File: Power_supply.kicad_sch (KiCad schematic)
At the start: 16 parts, among them J2 DC_DC_Buck_converter_module, U1 TPS562201DDCR

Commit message: wip
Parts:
- renumbered C74 to C14, C75 to C15, C76 to C16, C77 to C17, C78 to C18, C79 to C19, C80 to C20, L13 to L1, R41 to R5, R42 to R6, R43 to R7, R44 to R8
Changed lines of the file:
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@@
 		(on_board yes)
 		(dnp no)
-		(property "Reference" "#PWR0172"
+		(property "Reference" "#PWR064"
 			(at 55.88 88.9 0)
 			(effects
@@
 			(project "mgr_board"
 				(path "/14d3b6cb-e4ae-41db-89eb-e86b07bc47b0/1fa8a5b5-8827-4ec4-a071-93d7f03057ab"
-					(reference "#PWR0172")
+					(reference "#PWR064")
 					(unit 1)
 				)
@@
 		(dnp no)
 		(fields_autoplaced yes)
-		(property "Reference" "R43"
+		(property "Reference" "R7"
 			(at 151.13 87.6299 90)
 			(effects
@@
 			(project "mgr_board"
 				(path "/14d3b6cb-e4ae-41db-89eb-e86b07bc47b0/1fa8a5b5-8827-4ec4-a071-93d7f03057ab"
-					(reference "R43")
+					(reference "R7")
 					(unit 1)
 				)
@@
 		(dnp no)
 		(fields_autoplaced yes)
-		(property "Reference" "R42"
+		(property "Reference" "R6"
 			(at 96.52 97.7899 90)
 			(effects
@@
 			(project "mgr_board"
 				(path "/14d3b6cb-e4ae-41db-89eb-e86b07bc47b0/1fa8a5b5-8827-4ec4-a071-93d7f03057ab"
-					(reference "R42")
+					(reference "R6")
 					(unit 1)
 				)
@@
 		(on_board yes)
 		(dnp no)
-		(property "Reference" "C76"
+		(property "Reference" "C16"
 			(at 78.994 89.662 0)
 			(effects
@@
 			(project "mgr_board"
 				(path "/14d3b6cb-e4ae-41db-89eb-e86b07bc47b0/1fa8a5b5-8827-4ec4-a071-93d7f03057ab"
-					(reference "C76")
+					(reference "C16")
 					(unit 1)
 				)
@@
 		(dnp no)
 		(fields_autoplaced yes)
-		(property "Reference" "#PWR0173"
+		(property "Reference" "#PWR065"
 			(at 60.96 96.52 0)
 			(effects
@@
 			(project "mgr_board"
 				(path "/14d3b6cb-e4ae-41db-89eb-e86b07bc47b0/1fa8a5b5-8827-4ec4-a071-93d7f03057ab"
-					(reference "#PWR0173")
+					(reference "#PWR065")
 					(unit 1)
 				)
@@
 		(dnp no)
 		(fields_autoplaced yes)
-		(property "Reference" "#PWR0179"
+		(property "Reference" "#PWR071"
 			(at 114.3 101.6 0)
 			(effects
@@
 			(project "mgr_board"
 				(path "/14d3b6cb-e4ae-41db-89eb-e86b07bc47b0/1fa8a5b5-8827-4ec4-a071-93d7f03057ab"
-					(reference "#PWR0179")
+					(reference "#PWR071")
 					(unit 1)
 				)
@@
 		(on_board yes)
 		(dnp no)
-		(property "Reference" "#PWR0185"
+		(property "Reference" "#PWR077"
 			(at 190.5 88.9 0)
 			(effects
@@
 			(project "mgr_board"
 				(path "/14d3b6cb-e4ae-41db-89eb-e86b07bc47b0/1fa8a5b5-8827-4ec4-a071-93d7f03057ab"
-					(reference "#PWR0185")
+					(reference "#PWR077")
 					(unit 1)
 				)
@@
 		(dnp no)
 		(fields_autoplaced yes)
-		(property "Reference" "#PWR0183"
+		(property "Reference" "#PWR075"
 			(at 176.53 96.52 0)
 			(effects
@@
 			(project "mgr_board"
 				(path "/14d3b6cb-e4ae-41db-89eb-e86b07bc47b0/1fa8a5b5-8827-4ec4-a071-93d7f03057ab"
-					(reference "#PWR0183")
+					(reference "#PWR075")
 					(unit 1)
 				)
@@
 		(dnp no)
 		(fields_autoplaced yes)
-		(property "Reference" "R44"
+		(property "Reference" "R8"
 			(at 151.13 97.7899 90)
 			(effects
@@
 			(project "mgr_board"
 				(path "/14d3b6cb-e4ae-41db-89eb-e86b07bc47b0/1fa8a5b5-8827-4ec4-a071-93d7f03057ab"
-					(reference "R44")
+					(reference "R8")
 					(unit 1)
 				)
@@
 		(dnp no)
 		(fields_autoplaced yes)
-		(property "Reference" "#PWR0182"
+		(property "Reference" "#PWR074"
 			(at 166.37 96.52 0)
 			(effects
@@
 			(project "mgr_board"
 				(path "/14d3b6cb-e4ae-41db-89eb-e86b07bc47b0/1fa8a5b5-8827-4ec4-a071-93d7f03057ab"
-					(reference "#PWR0182")
+					(reference "#PWR074")
 					(unit 1)
 				)
@@
 		(on_board yes)
 		(dnp no)
-		(property "Reference" "C74"
+		(property "Reference" "C14"
 			(at 56.388 89.662 0)
 			(effects
@@
 			(project "mgr_board"
 				(path "/14d3b6cb-e4ae-41db-89eb-e86b07bc47b0/1fa8a5b5-8827-4ec4-a071-93d7f03057ab"
-					(reference "C74")
+					(reference "C14")
 					(unit 1)
 				)
@@
 		(on_board yes)
 		(dnp no)
-		(property "Reference" "C80"
+		(property "Reference" "C20"
 			(at 194.056 88.646 0)
 			(effects
@@
 			(project "mgr_board"
 				(path "/14d3b6cb-e4ae-41db-89eb-e86b07bc47b0/1fa8a5b5-8827-4ec4-a071-93d7f03057ab"
-					(reference "C80")
+					(reference "C20")
 					(unit 1)
 				)
@@
 		(on_board yes)
 		(dnp no)
-		(property "Reference" "#PWR0180"
+		(property "Reference" "#PWR072"
 			(at 121.92 67.31 0)
 			(effects
@@
 			(project "mgr_board"
 				(path "/14d3b6cb-e4ae-41db-89eb-e86b07bc47b0/1fa8a5b5-8827-4ec4-a071-93d7f03057ab"
-					(reference "#PWR0180")
+					(reference "#PWR072")
 					(unit 1)
 				)
@@
 		(dnp no)
 		(fields_autoplaced yes)
-		(property "Reference" "#PWR0175"
+		(property "Reference" "#PWR067"
 			(at 83.82 96.52 0)
 			(effects
@@
 			(project "mgr_board"
 				(path "/14d3b6cb-e4ae-41db-89eb-e86b07bc47b0/1fa8a5b5-8827-4ec4-a071-93d7f03057ab"
-					(reference "#PWR0175")
+					(reference "#PWR067")
 					(unit 1)
 				)
@@
 		(dnp no)
 		(fields_autoplaced yes)
-		(property "Reference" "#PWR0184"
+		(property "Reference" "#PWR076"
 			(at 186.69 96.52 0)
 			(effects
@@
 			(project "mgr_board"
 				(path "/14d3b6cb-e4ae-41db-89eb-e86b07bc47b0/1fa8a5b5-8827-4ec4-a071-93d7f03057ab"
-					(reference "#PWR0184")
+					(reference "#PWR076")
 					(unit 1)
 				)
@@
 		(on_board yes)
 		(dnp no)
-		(property "Reference" "C77"
+		(property "Reference" "C17"
 			(at 138.684 91.186 0)
 			(effects
@@
 			(project "mgr_board"
 				(path "/14d3b6cb-e4ae-41db-89eb-e86b07bc47b0/1fa8a5b5-8827-4ec4-a071-93d7f03057ab"
-					(reference "C77")
+					(reference "C17")
 					(unit 1)
 				)
@@
 		(on_board yes)
 		(dnp no)
-		(property "Reference" "C78"
+		(property "Reference" "C18"
 			(at 172.974 88.9 0)
 			(effects
@@
 			(project "mgr_board"
 				(path "/14d3b6cb-e4ae-41db-89eb-e86b07bc47b0/1fa8a5b5-8827-4ec4-a071-93d7f03057ab"
-					(reference "C78")
+					(reference "C18")
 					(unit 1)
 				)
@@
 		(dnp no)
 		(fields_autoplaced yes)
-		(property "Reference" "#PWR0174"
+		(property "Reference" "#PWR066"
 			(at 71.12 96.52 0)
 			(effects
@@
 			(project "mgr_board"
 				(path "/14d3b6cb-e4ae-41db-89eb-e86b07bc47b0/1fa8a5b5-8827-4ec4-a071-93d7f03057ab"
-					(reference "#PWR0174")
+					(reference "#PWR066")
 					(unit 1)
 				)
@@
 		(dnp no)
 		(fields_autoplaced yes)
-		(property "Reference" "#PWR0178"
+		(property "Reference" "#PWR070"
 			(at 114.3 72.39 0)
 			(effects
@@
 			(project "mgr_board"
 				(path "/14d3b6cb-e4ae-41db-89eb-e86b07bc47b0/1fa8a5b5-8827-4ec4-a071-93d7f03057ab"
-					(reference "#PWR0178")
+					(reference "#PWR070")
 					(unit 1)
 				)
@@
 		(on_board yes)
 		(dnp no)
-		(property "Reference" "#PWR0177"
+		(property "Reference" "#PWR069"
 			(at 106.68 67.31 0)
 			(effects
@@
 			(project "mgr_board"
 				(path "/14d3b6cb-e4ae-41db-89eb-e86b07bc47b0/1fa8a5b5-8827-4ec4-a071-93d7f03057ab"
-					(reference "#PWR0177")
+					(reference "#PWR069")
 					(unit 1)
 				)
@@
 		(dnp no)
 		(fields_autoplaced yes)
-		(property "Reference" "L13"
+		(property "Reference" "L1"
 			(at 139.7 80.01 90)
 			(effects
@@
 			(project ""
 				(path "/14d3b6cb-e4ae-41db-89eb-e86b07bc47b0/1fa8a5b5-8827-4ec4-a071-93d7f03057ab"
-					(reference "L13")
+					(reference "L1")
 					(unit 1)
 				)
@@
 		(on_board yes)
 		(dnp no)
-		(property "Reference" "C79"
+		(property "Reference" "C19"
 			(at 182.88 89.408 0)
 			(effects
@@
 			(project "mgr_board"
 				(path "/14d3b6cb-e4ae-41db-89eb-e86b07bc47b0/1fa8a5b5-8827-4ec4-a071-93d7f03057ab"
-					(reference "C79")
+					(reference "C19")
 					(unit 1)
 				)
@@
 		(dnp no)
 		(fields_autoplaced yes)
-		(property "Reference" "#PWR0176"
+		(property "Reference" "#PWR068"
 			(at 93.98 109.22 0)
 			(effects
@@
 			(project "mgr_board"
 				(path "/14d3b6cb-e4ae-41db-89eb-e86b07bc47b0/1fa8a5b5-8827-4ec4-a071-93d7f03057ab"
-					(reference "#PWR0176")
+					(reference "#PWR068")
 					(unit 1)
 				)
@@
 		(on_board yes)
 		(dnp no)
-		(property "Reference" "C75"
+		(property "Reference" "C15"
 			(at 67.056 89.662 0)
 			(effects
@@
 			(project "mgr_board"
 				(path "/14d3b6cb-e4ae-41db-89eb-e86b07bc47b0/1fa8a5b5-8827-4ec4-a071-93d7f03057ab"
-					(reference "C75")
+					(reference "C15")
 					(unit 1)
 				)
@@
 		(dnp no)
 		(fields_autoplaced yes)
-		(property "Reference" "#PWR0181"
+		(property "Reference" "#PWR073"
 			(at 148.59 109.22 0)
 			(effects
@@
 			(project "mgr_board"
 				(path "/14d3b6cb-e4ae-41db-89eb-e86b07bc47b0/1fa8a5b5-8827-4ec4-a071-93d7f03057ab"
-					(reference "#PWR0181")
+					(reference "#PWR073")
 					(unit 1)
 				)
@@
 		(dnp no)
 		(fields_autoplaced yes)
-		(property "Reference" "R41"
+		(property "Reference" "R5"
 			(at 96.52 87.6299 90)
 			(effects
@@
 			(project "mgr_board"
 				(path "/14d3b6cb-e4ae-41db-89eb-e86b07bc47b0/1fa8a5b5-8827-4ec4-a071-93d7f03057ab"
-					(reference "R41")
-					(unit 1)
-				)
+					(reference "R5")
+					(unit 1)
+				)

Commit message: wip
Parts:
- removed J2: DC_DC_Buck_converter_module, Connector_PinHeader_2.54mm:PinHeader_1x03_P2.54mm_Vertical, symbol PCM_SL_Pin_Headers:PINHD_1x3_Male
- added U2: LM2596 BUCK MODULE, footprint_lib:LM2596 DC-DC module, symbol sym_lib:DC-DC_Step_down_module
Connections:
- net +12V: now also U2.1 (IN+)
- net +5V: now also U2.3 (OUT+)
- net GND: now also U2.2 (IN-), U2.4 (OUT-)
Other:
- note added: "OPTIONAL"

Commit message: finished boarD
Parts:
- removed TP21: TestPoint, TestPoint:TestPoint_Pad_D2.0mm, symbol Connector:TestPoint
- added C83, C84: 100uF, Capacitor_SMD:CP_Elec_6.3x7.7, symbol Device:C_Polarized_Small
- C14, C18: LCSC (none) -> C96446
- C15, C19: LCSC (none) -> C45783
- C16, C17, C20: LCSC (none) -> C14663
- L1: LCSC (none) -> C408410
- R5, R6, R8: LCSC (none) -> C25804
- R7: value 54,9k -> 56k; LCSC (none) -> C23206
- U1: LCSC (none) -> C90061
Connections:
- net +12V: now also C83.1, C84.1
- net GND: now also C83.2, C84.2

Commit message: Fixed bugs after reviews
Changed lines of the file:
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@@
 					(size 1.27 1.27)
 				)
+				(hide yes)
 			)
 		)
@@
 					(size 1.27 1.27)
 				)
+				(hide yes)
 			)
 		)
@@
 					(size 1.27 1.27)
 				)
+				(hide yes)
 			)
 		)
@@
 					(size 1.27 1.27)
 				)
+				(hide yes)
 			)
 		)
@@
 					(size 1.27 1.27)
 				)
+				(hide yes)
 			)
 		)
@@
 					(size 1.27 1.27)
 				)
+				(hide yes)
 			)
 		)
@@
 					(size 1.27 1.27)
 				)
+				(hide yes)
 			)
 		)
@@
 					(size 1.27 1.27)
 				)
+				(hide yes)
 			)
 		)
@@
 					(size 1.27 1.27)
 				)
+				(hide yes)
 			)
 		)
@@
 					(size 1.27 1.27)
 				)
+				(hide yes)
 			)
 		)
@@
 					(size 1.27 1.27)
 				)
+				(hide yes)
 			)
 		)
@@
 					(size 1.27 1.27)
 				)
-			)
-		)
+				(hide yes)
+			)
+		)

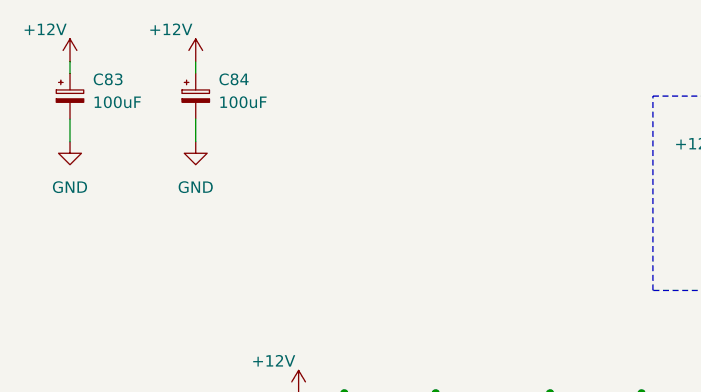
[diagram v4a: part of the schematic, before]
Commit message: Added current sense amplifier, reduced one ADC, changed elec cap to tantals, to review
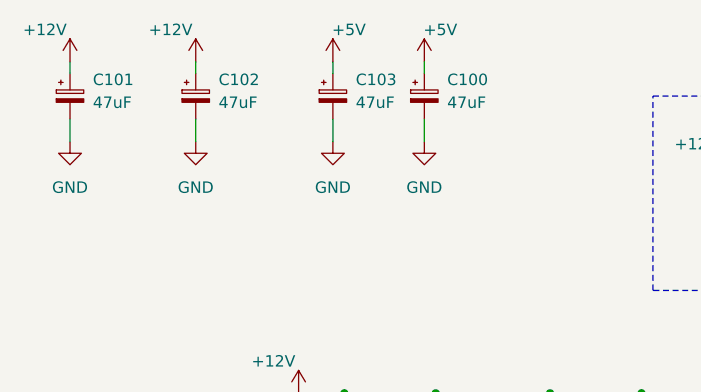
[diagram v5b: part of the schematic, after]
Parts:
- removed C83, C84: 100uF, Capacitor_SMD:CP_Elec_6.3x7.7, symbol Device:C_Polarized_Small
- added C100, C101, C102, C103: 47uF, Capacitor_Tantalum_SMD:CP_EIA-6032-15_Kemet-U_Pad2.25x2.35mm_HandSolder, symbol Device:C_Polarized_Small
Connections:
- net +12V: now also C101.1, C102.1
- net +5V: now also C100.1, C103.1
- net GND: now also C100.2, C101.2, C102.2, C103.2
